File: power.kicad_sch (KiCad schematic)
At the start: 44 parts, among them J2 UJ20-C-H-G-SMT-1-P16-TR, U2 MCP73871, U3 AP2112K-3.3, U4 MAX17048G_T10, U5 USBLC6-2SC6, U9 USBLC6-2SC6

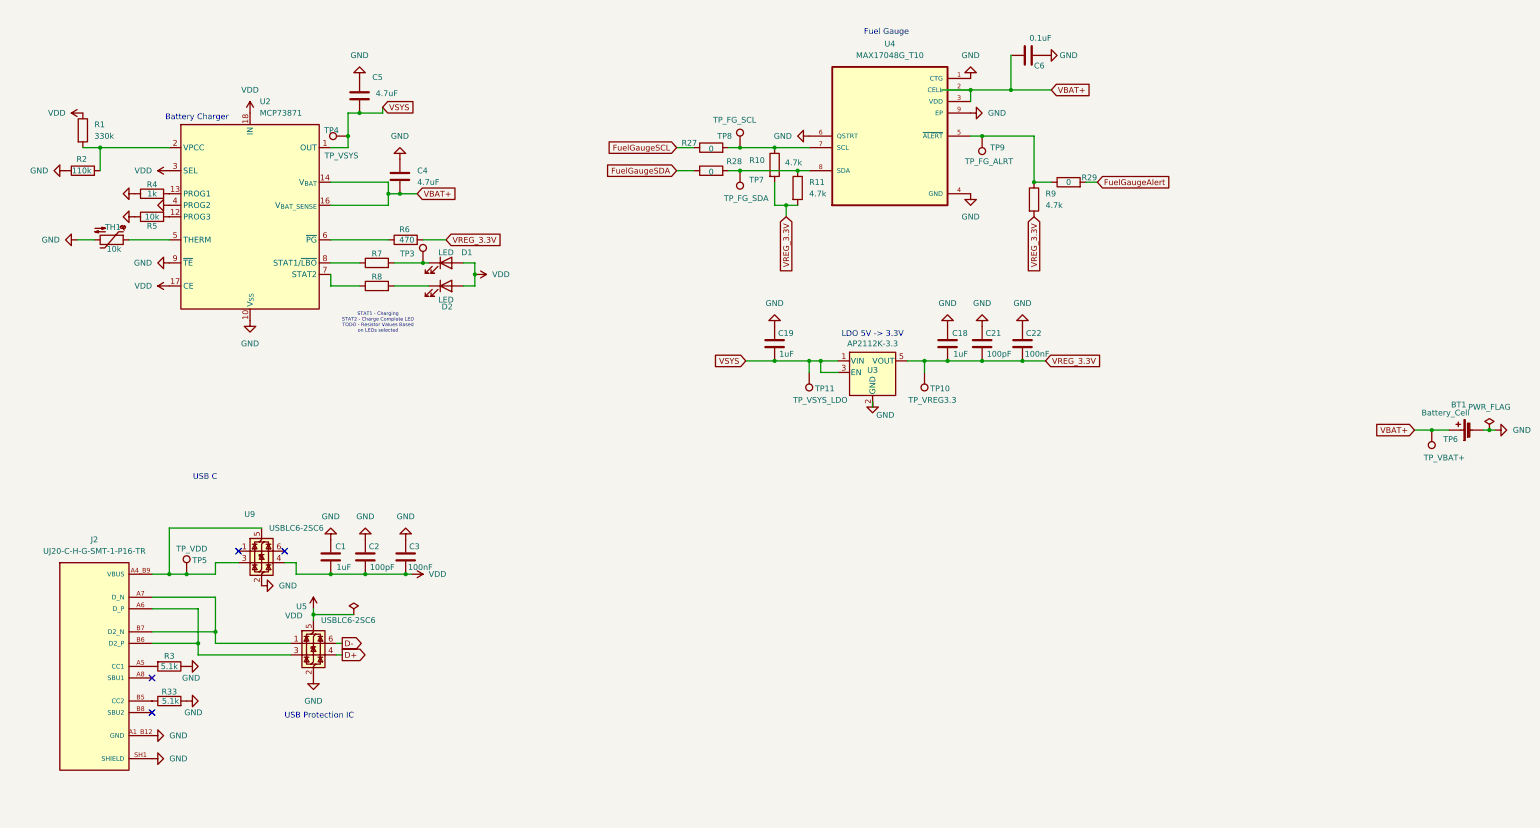
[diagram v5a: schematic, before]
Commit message: Add 3d models and design rules
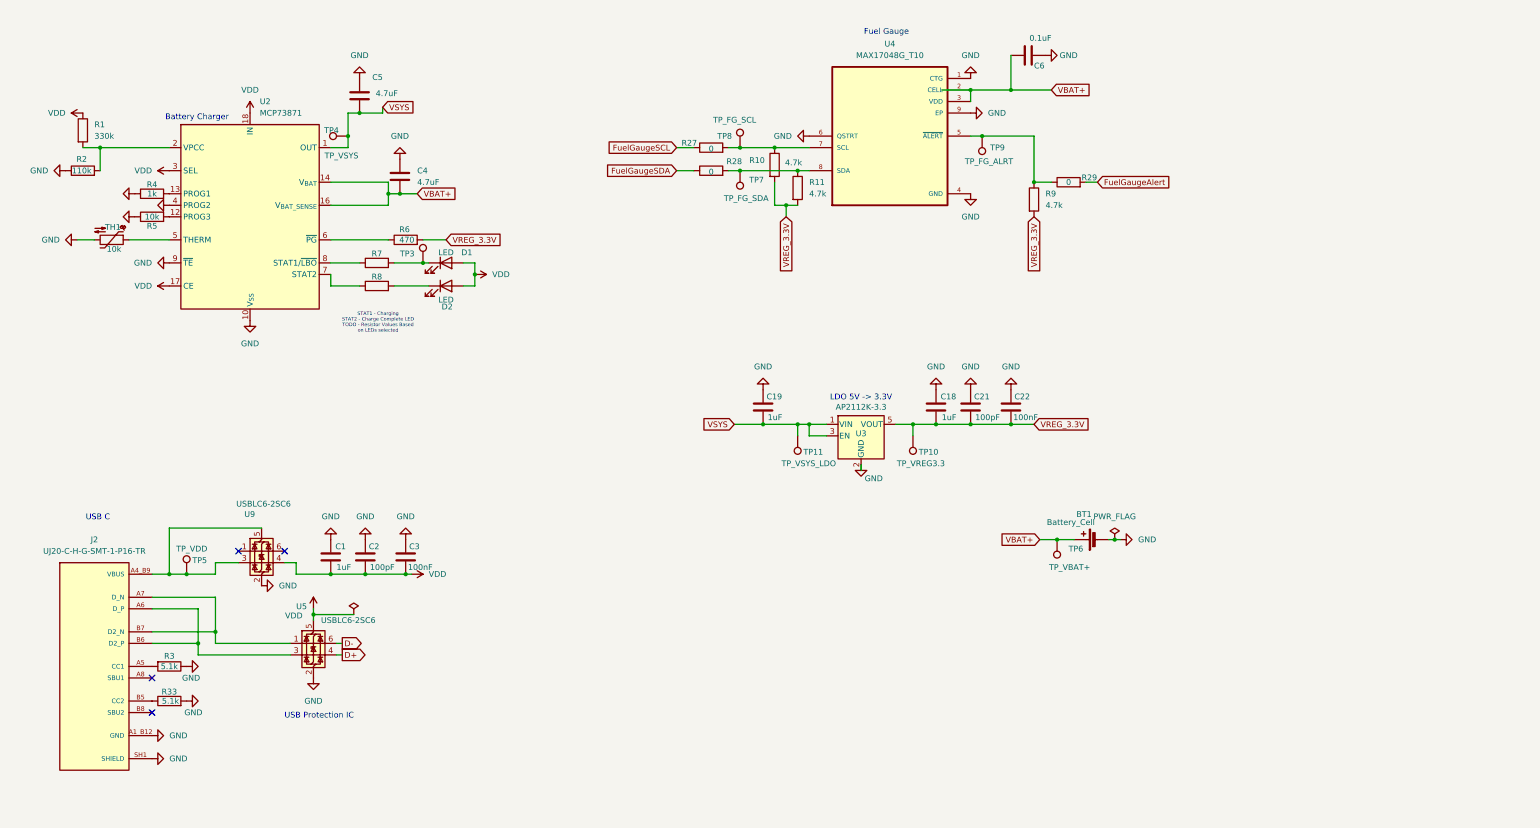
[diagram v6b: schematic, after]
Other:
- moved on the sheet: BT1, C18, C19, C21, C22, TP10, TP11, TP6, U3

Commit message: Update speaker PCB design
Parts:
- removed U9: USBLC6-2SC6, Package_TO_SOT_SMD:SOT-23-6, symbol Power_Protection:USBLC6-2SC6
- renumbered TP11 to TP_VSYS_LDO
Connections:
- net VDD: now also J2.A4_B9 (VBUS), J2.B4_A9 (VBUS), TP5.1
- no-connect marks 4 -> 2
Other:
- moved on the sheet: C1, C2, C3, C4, C6, D2, R10, R11, R4, R5, R6, R8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

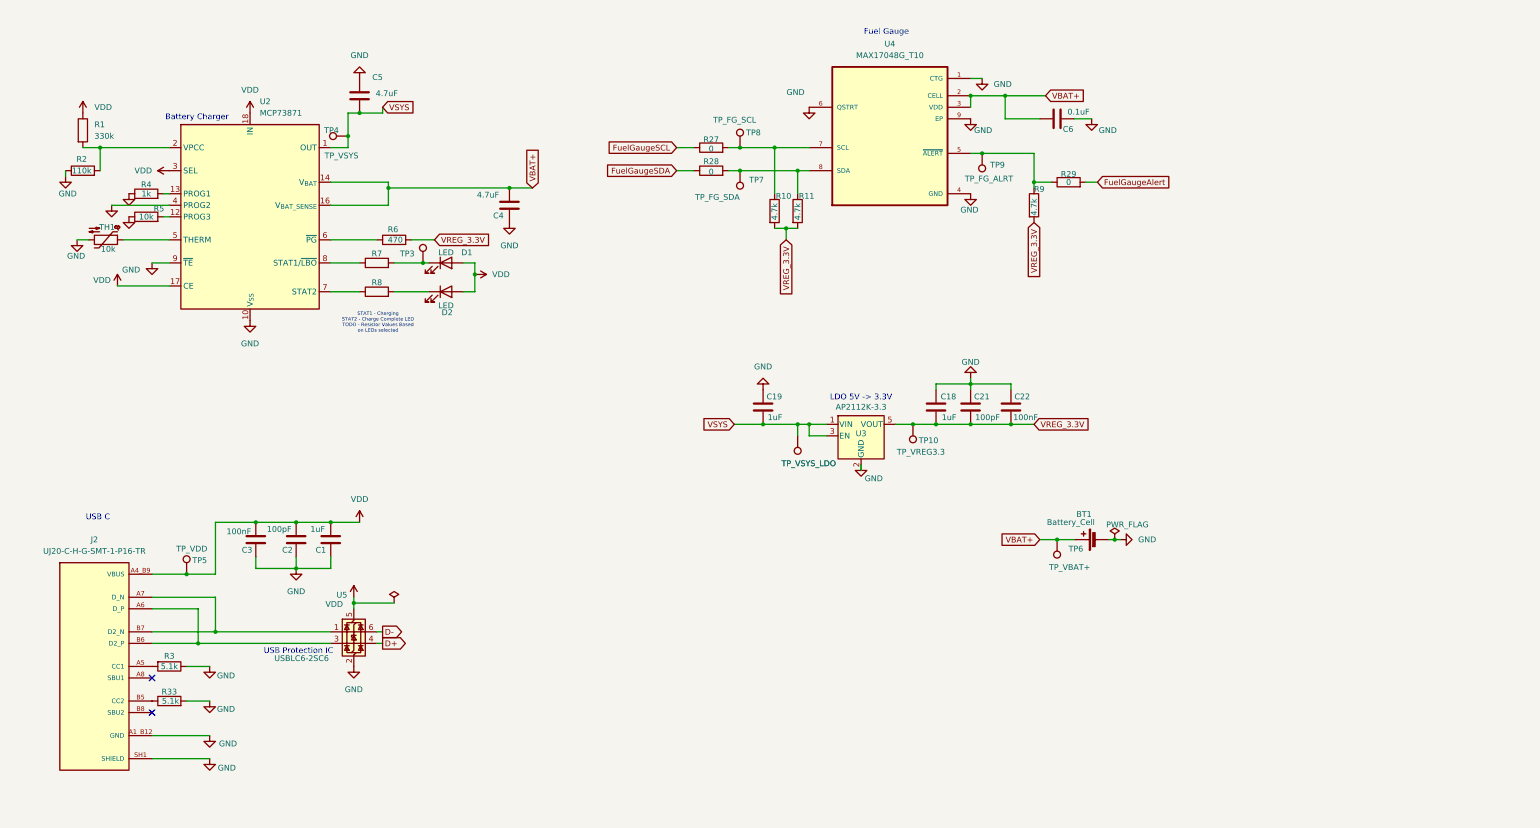
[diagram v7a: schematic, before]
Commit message: Update LDO and make some visual tweaks suggested by conor
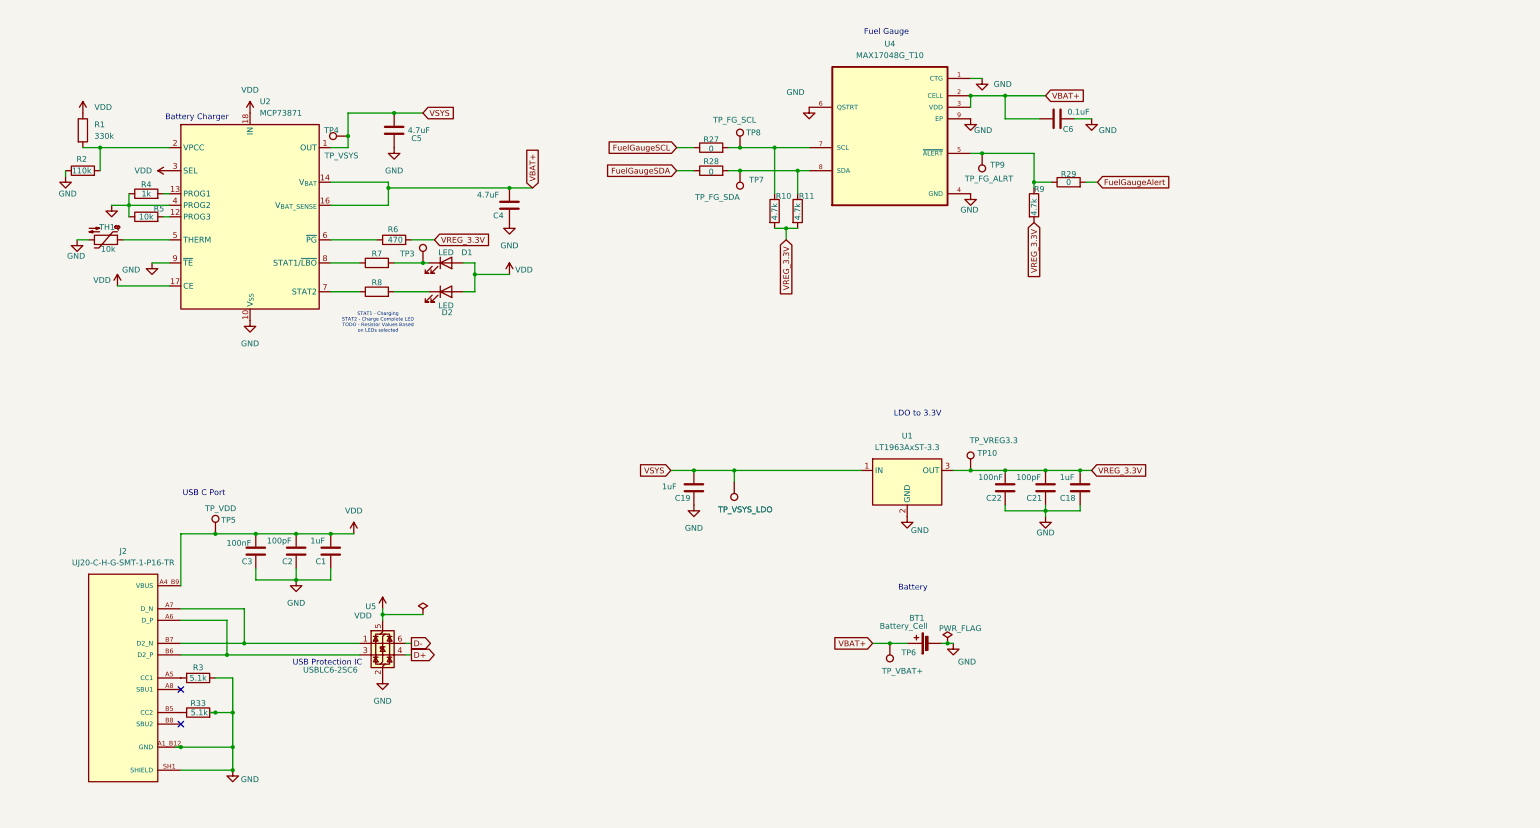
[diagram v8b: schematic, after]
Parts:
- removed U3: AP2112K-3.3, Package_TO_SOT_SMD:SOT-23-5, symbol Regulator_Linear:AP2112K-3.3
- added U1: LT1963AxST-3.3, Package_TO_SOT_SMD:SOT-223-3_TabPin2, symbol Regulator_Linear:LT1963AxST-3.3
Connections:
- net GND: now also U1.2 (GND)
- net VREG_3.3V: now also U1.3 (OUT)
- net VSYS: now also U1.1 (IN)
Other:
- note added: "Battery"
- note added: "LDO to 3.3V"
- note added: "USB C Port"
- note removed: "LDO 5V -> 3.3V"
- note removed: "USB C"
- moved on the sheet: BT1, C1, C18, C19, C2, C21, C22, C3, C5, J2, R3, R33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
